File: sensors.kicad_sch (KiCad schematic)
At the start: 2 parts, among them U2 AHT20, U3 BMP280

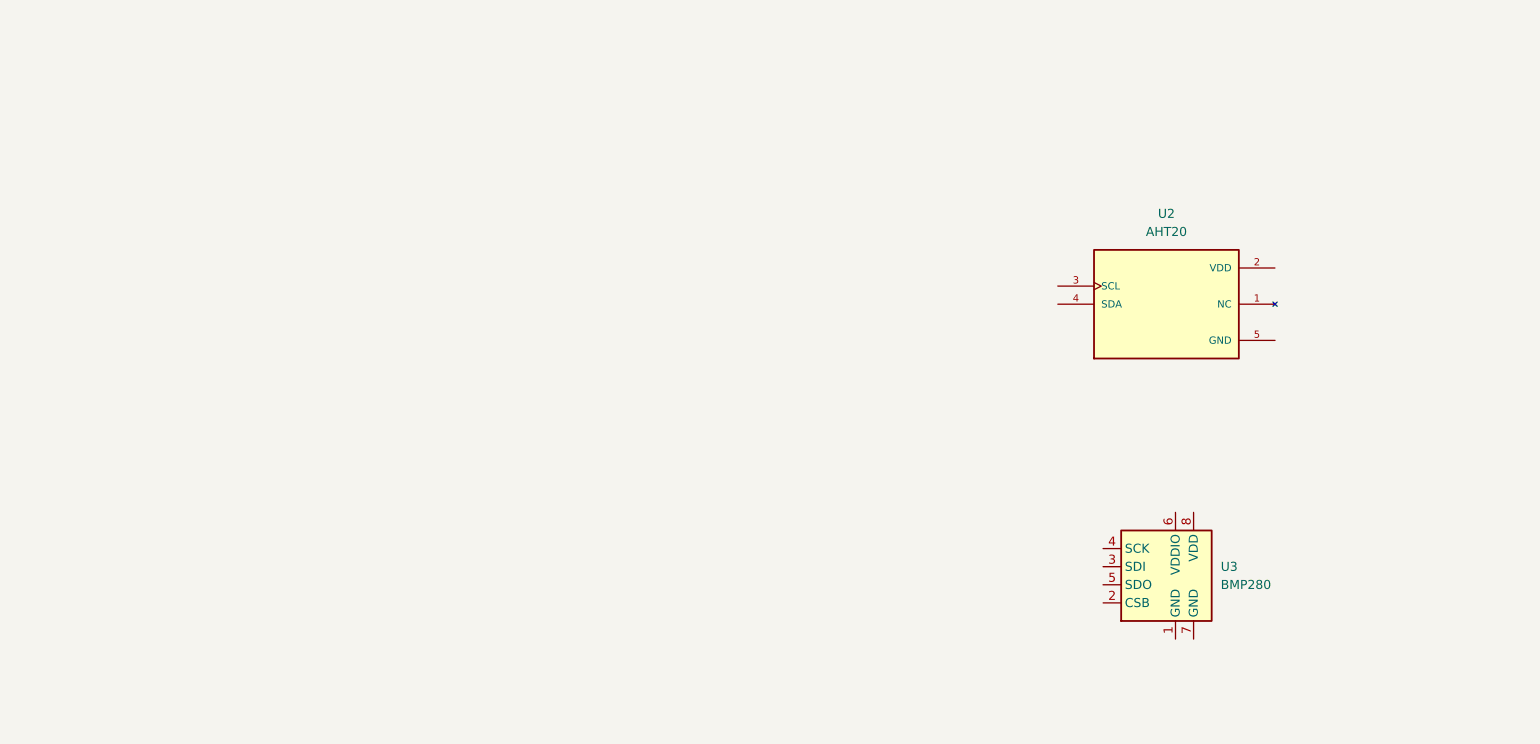
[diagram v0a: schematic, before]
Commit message: Current version of BMP280 schematic
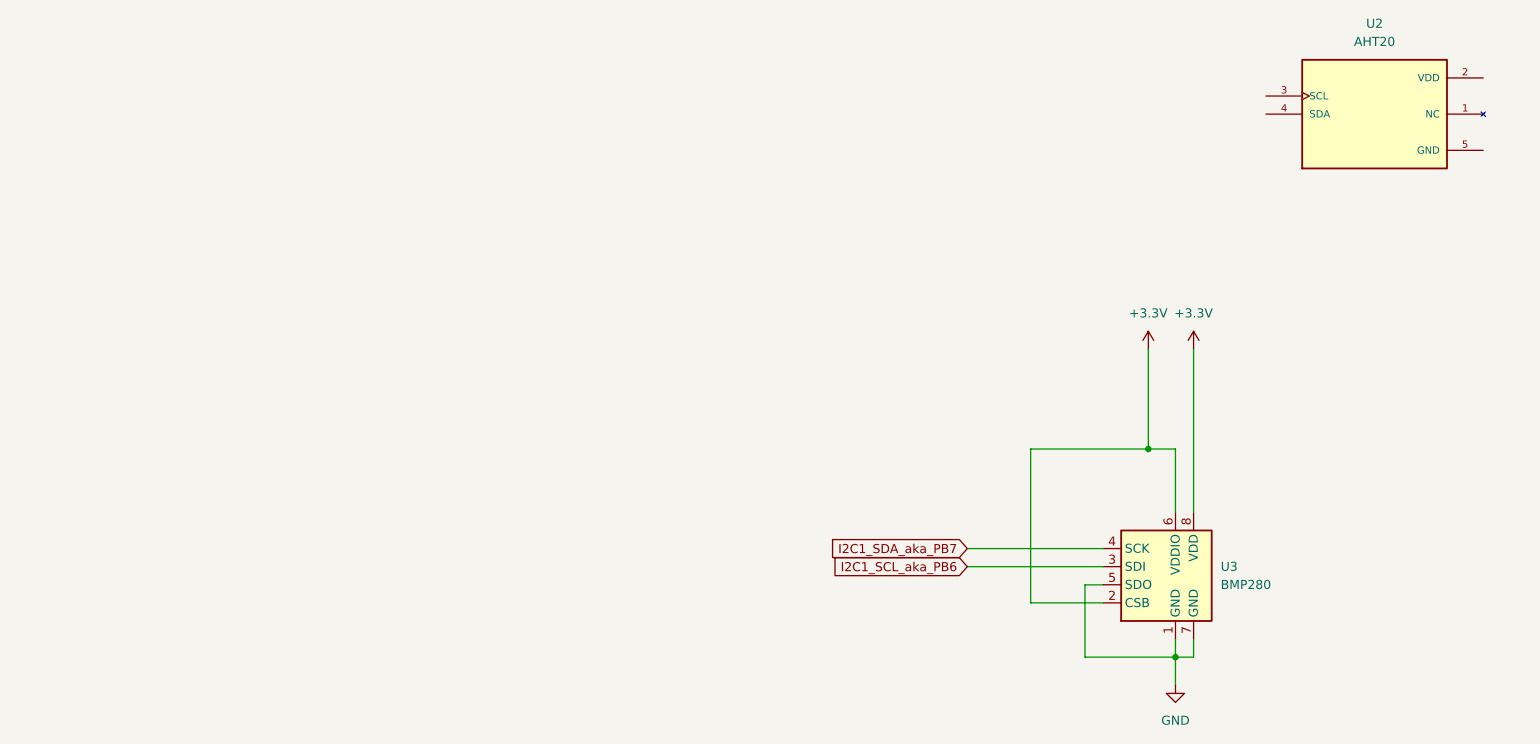
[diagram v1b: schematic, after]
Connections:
- net GND: now reaches U3.1 (GND)
- net GND: now also U3.5 (SDO), U3.7 (GND)
- net +3.3V: now reaches U3.2 (CSB)
- net +3.3V: now also U3.6 (VDDIO), U3.8 (VDD)
- net I2C1_SCL_aka_PB6: now reaches U3.3 (SDI)
- net I2C1_SDA_aka_PB7: now reaches U3.4 (SCK)
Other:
- moved on the sheet: U2

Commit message: Made BME280 IC schematic
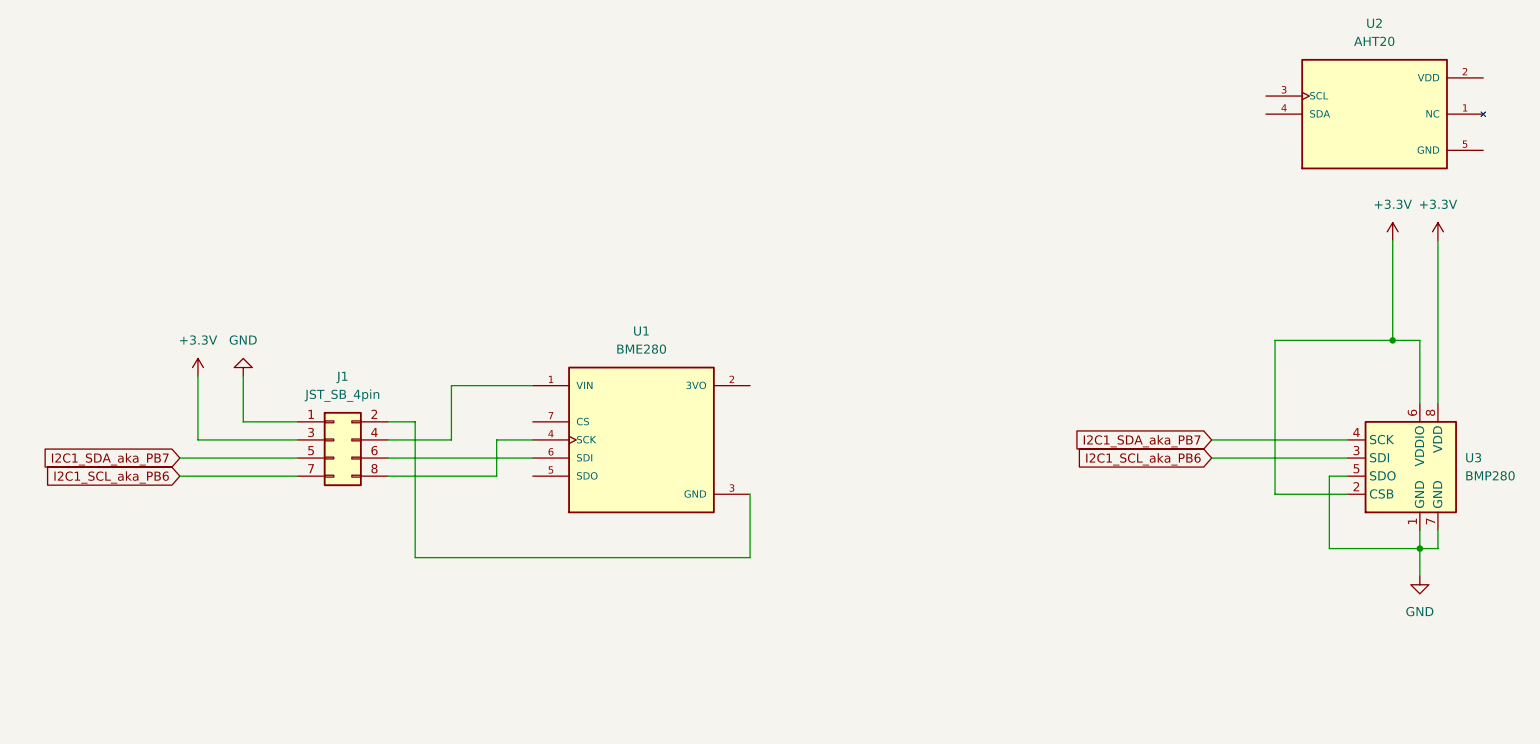
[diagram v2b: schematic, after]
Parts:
- added J1: JST_SB_4pin, Connector_JST:JST_SH_SM04B-SRSS-TB_1x04-1MP_P1.00mm_Horizontal, symbol Connector_Generic:Conn_02x04_Odd_Even
- added U1: BME280, SuperDoppler2000:BME280Footprint, symbol adafruitBME280:2652
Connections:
- net +3.3V: now also J1.3 (Pin_3)
- net GND: now also J1.1 (Pin_1)
- net I2C1_SCL_aka_PB6: now also J1.7 (Pin_7)
- net I2C1_SDA_aka_PB7: now also J1.5 (Pin_5)
- new net: J1.4 (Pin_4), U1.1 (VIN)
- new net: J1.2 (Pin_2), U1.3 (GND)
- new net: J1.8 (Pin_8), U1.4 (SCK)
- new net: J1.6 (Pin_6), U1.6 (SDI)
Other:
- moved on the sheet: U3
